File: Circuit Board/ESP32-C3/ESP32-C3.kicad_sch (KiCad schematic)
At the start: 48 parts, among them IC1 W25Q16JVUXIQ_TR, J1 Conn_01x04_Male, J2 USB_C_Receptacle_USB2.0, SW1 SW_Push, SW2 SW_Push, U1 USBLC6-2SC6, U2 ESP32-C3, U3 USBLC6-2SC6, U4 SPX3819M5-L-3-3

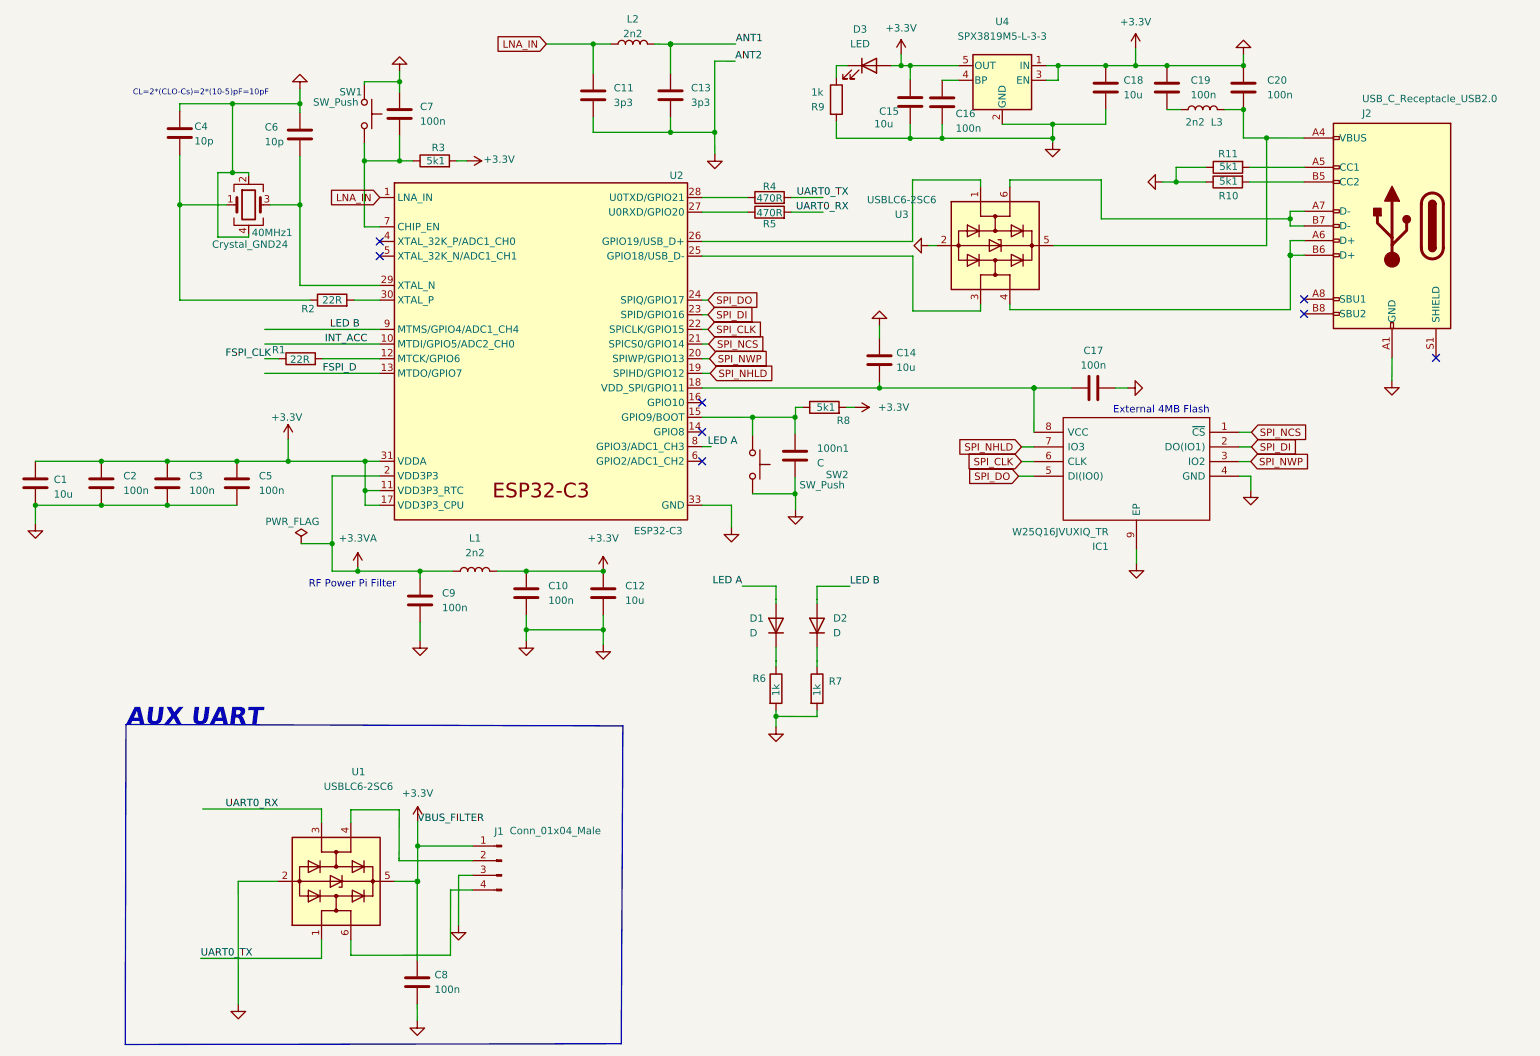
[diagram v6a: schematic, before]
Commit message: Started PCB routing
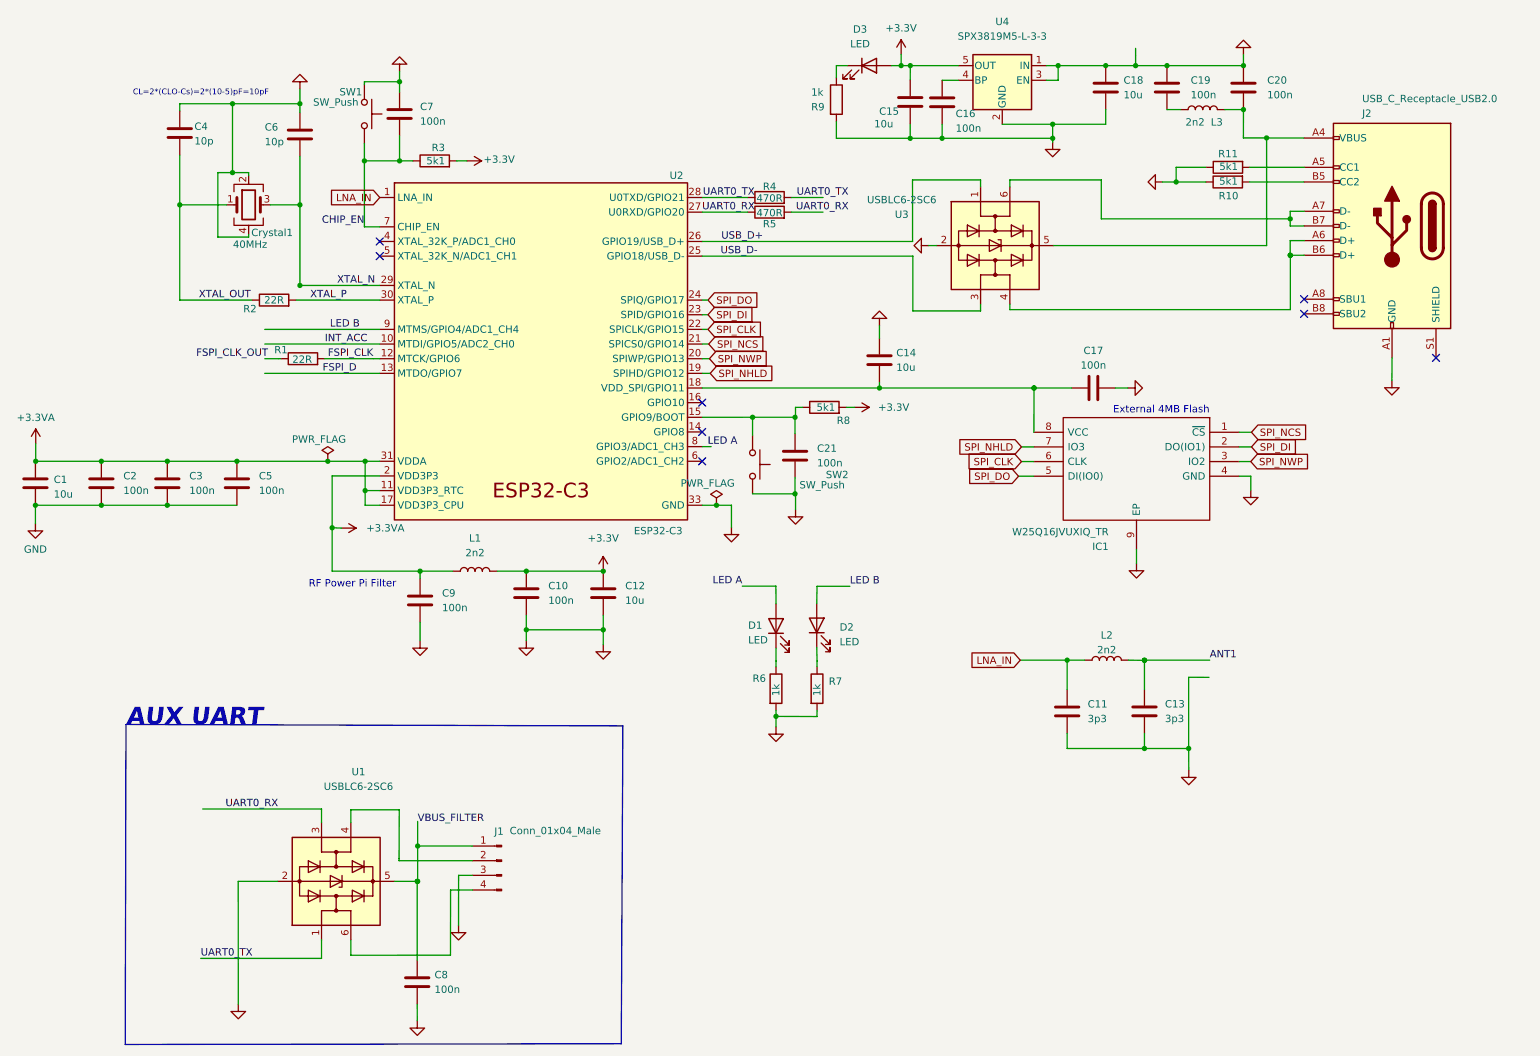
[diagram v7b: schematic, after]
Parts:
- removed D1, D2: D, symbol Device:D
- added D1, D2: LED, LED_SMD:LED_0603_1608Metric, symbol Device:LED
- C1, C12, C14, C15, C18: footprint (none) -> Capacitor_SMD:C_0603_1608Metric
- C10, C11, C13, C16, C17, C19, C2, C20, C3, C4, C5, C6, C7, C8, C9: footprint (none) -> Capacitor_SMD:C_0402_1005Metric
- C21: renamed from 100n1; value C -> 100n; footprint (none) -> Capacitor_SMD:C_0402_1005Metric
- Crystal1: renamed from 40MHz1; value Crystal_GND24 -> 40MHz; footprint (none) -> Crystal:Crystal_SMD_3225-4Pin_3.2x2.5mm_HandSoldering
- D3: footprint (none) -> LED_SMD:LED_0603_1608Metric
- IC1: footprint SON50P300X200X60-9N -> W25Q16JVUXIQ_TR:SON50P300X200X60-9N
- J2: footprint (none) -> Connector_USB:USB_C_Receptacle_HRO_TYPE-C-31-M-12
- L1, L2, L3: footprint (none) -> Inductor_SMD:L_0603_1608Metric
- R1, R10, R11, R2, R3, R4, R5, R6, R7, R8, R9: footprint (none) -> Resistor_SMD:R_0402_1005Metric
- SW1, SW2: footprint (none) -> Button_Switch_SMD:SW_SPST_B3U-1000P
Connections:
- net +3.3V: no longer C1.1, C1.2, C10.2, C11.2, C12.2, C13.2, C14.1, C15.2, C16.2, C17.2, C18.1, C18.2, C19.1, C2.1, C2.2, C20.1, C21.2, C3.1, C3.2, C4.1, C5.1, C5.2, C6.1, C7.1, C8.1, C8.2, C9.2, Crystal1.2, Crystal1.4, IC1.4 (GND), IC1.9 (EP), J1.1 (Pin_1), J1.3 (Pin_3), J2.A1 (GND), J2.A12 (GND), J2.B1 (GND), J2.B12 (GND), R10.1, R11.1, R6.2, R7.2, R9.2, SW1.1, SW2.2, U1.2 (GND), U1.5 (VBUS), U2.11 (VDD3P3_RTC), U2.17 (VDD3P3_CPU), U2.31 (VDDA), U2.32 (VDDA), U2.33 (GND), U3.2 (GND), U4.1 (IN), U4.2 (GND), U4.3 (EN)
- net +3.3VA: now also C1.1, C2.1, C3.1, C5.1, U2.11 (VDD3P3_RTC), U2.17 (VDD3P3_CPU), U2.31 (VDDA), U2.32 (VDDA)
- net FSPI_CLK: now also R1.2, U2.12 (MTCK/GPIO6); no longer R1.1
- net LED A: now also D1.2 (A)
- net LED B: now also D2.2 (A)
- net UART0_RX: now also R5.1, U2.27 (U0RXD/GPIO20)
- net UART0_TX: now also R4.1, U2.28 (U0TXD/GPIO21)
- net at R6.1: now also D1.1 (K)
- net USB_D+: now reaches U2.26 (GPIO19/USB_D+), U3.1 (I/O1)
- net USB_D-: now reaches U2.25 (GPIO18/USB_D-), U3.3 (I/O2)
- net at R7.1: now also D2.1 (K)
- net XTAL_N: now reaches C6.2, Crystal1.3, U2.29 (XTAL_N)
- net XTAL_P: now reaches R2.2, U2.30 (XTAL_P)
- net CHIP_EN: now reaches C7.2, R3.1, SW1.2, U2.7 (CHIP_EN)
- net XTAL_OUT: now reaches C4.2, Crystal1.1, R2.1
- new net FSPI_CLK_OUT: R1.1
- new net GND: C1.2, C10.2, C11.2, C12.2, C13.2, C14.1, C15.2, C16.2, C17.2, C18.1, C18.2, C19.1, C2.2, C20.1, C21.2, C3.2, C4.1, C5.2, C6.1, C7.1, C8.2, C9.2, Crystal1.2, Crystal1.4, IC1.4 (GND), IC1.9 (EP), J1.3 (Pin_3), J2.A1 (GND), J2.A12 (GND), J2.B1 (GND), J2.B12 (GND), R10.1, R11.1, R6.2, R7.2, R9.2, SW1.1, SW2.2, U1.2 (GND), U2.33 (GND), U3.2 (GND), U4.1 (IN), U4.2 (GND), U4.3 (EN)
- new net VBUS_FILTER: C8.1, J1.1 (Pin_1), U1.5 (VBUS)
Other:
- moved on the sheet: C11, C13, L2, R2

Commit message: Finished PCB Layout v1.0
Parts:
- added ANT1: ESP32_Antenna, ESP32 Ant:ESPRESSIF_ESP32_MIFA_2.4GHz_Right, symbol Device:ESP32_Antenna
- added H1, H2, H3, H4: MountingHole, MountingHole:MountingHole_2.2mm_M2, symbol Mechanical:MountingHole
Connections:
- net ANT1: now also ANT1.1 (Feed)
- net GND: now also C19.2, C20.2, ANT1.2 (GND); no longer C18.1, C19.1, C20.1, U4.1 (IN), U4.3 (EN)
- net D+: now reaches J2.A6 (D+), J2.B6 (D+), U3.4 (I/O2)
- net VBUS: now reaches J2.A4 (VBUS), J2.A9 (VBUS), J2.B4 (VBUS), J2.B9 (VBUS), L3.2, U3.5 (VBUS)
- net VBUS: now also C20.1; no longer C20.2
- net D-: now reaches J2.A7 (D-), J2.B7 (D-), U3.6 (I/O1)
- net BOOT: now reaches C21.1, R8.1, SW2.1, U2.15 (GPIO9/BOOT)
- net VDD_SPI: now reaches C14.2, C17.1, IC1.8 (VCC), U2.18 (VDD_SPI/GPIO11)
- net VBUS FILT: now reaches L3.1
- net VBUS FILT: now also C18.1, C19.1, U4.1 (IN), U4.3 (EN); no longer C19.2
- net CC2: now reaches J2.B5 (CC2), R10.2
- net CC1: now reaches J2.A5 (CC1), R11.2
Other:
- moved on the sheet: L3
